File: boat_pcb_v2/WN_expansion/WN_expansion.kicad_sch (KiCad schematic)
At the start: 3 parts, among them J16 TSW-108-07-F-D, J17 TSW-108-07-F-D, J18 TSW-108-07-F-D

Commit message: cleaned up expansion board
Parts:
- added C20, C26: 1µ, 100V, WaterNet Footprints:CAPC2012X145N, symbol Device:C
- added C27, C28: 1µ, 25V, WaterNet26 Footprints:CAPC2012X145N, symbol Device:C
- added D4: USBLC6-2SC6, Package_TO_SOT_SMD:SOT-23-6, symbol Power_Protection:USBLC6-2SC6
- added J1, J2: Conn_02x10_Odd_Even, symbol Connector_Generic:Conn_02x10_Odd_Even
- added J19: TSW-108-07-F-D, WaterNet26 Library:SAMTEC_TSW-108-07-F-D, symbol WaterNet26 Library:TSW-108-07-F-D
- added J20: USB4120-03-C_REVA6, WaterNet26 Footprints:GCT_USB4120-03-C_REVA6, symbol WaterNet26 Library:USB4120-03-C_REVA6
- added JP2, JP3: B04B-PASK-1, WaterNet Footprints:B04B-PASK-1, symbol WaterNet Library:B04B-PASK-1_1
- added L6: 3.3µ, WaterNet26 Footprints:INDC1608X95N, symbol Device:L
- added R25, R26: 5.1K, WaterNet26 Footprints:RESC1508X55N, symbol WaterNet26 Library:RMCF0603FT5K10
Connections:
- net +3.3V: now also J18.02, J18.06, J18.10, J18.14
- net GND: now also J18.01, J18.05, J18.09, J18.13, C20.2, C26.2, C27.2, C28.2, D4.2 (GND), J20.A1 (GND_A), J20.A12 (GND_A), J20.B1 (GND_B), J20.B12 (GND_B), J20.S1 (SHIELD), J20.S2 (SHIELD), J20.S3 (SHIELD), J20.S4 (SHIELD), JP2.1, JP3.1, R25.1, R26.1
- net SDA: now reaches J18.03
- net SDA: now also J18.07, J18.11, J18.15
- net SCL: now reaches J18.04
- net SCL: now also J18.08, J18.12, J18.16
- new net: D4.1 (I/O1), J20.A7 (D1-), J20.B7 (D2-)
- new net: D4.3 (I/O2), J20.A6 (D1+), J20.B6 (D2+)
- new net: J20.A5 (CC1), R25.2
- new net: J20.B5 (CC2), R26.2
- new net +12ACC: J19.01, J19.02, J19.03, J19.04, J19.05, J19.06, J19.07, J19.08, J19.09, J19.10, J19.11, J19.12, J19.13, J19.14, J19.15, J19.16
- new net +3V3: C20.1, C26.1, JP2.2, JP3.2
- new net +VBUSF_1: C28.1, L6.2
- new net I2C1_SCL: JP2.4, JP3.4
- new net I2C1_SDA: JP2.3, JP3.3
- new net USB_D+: D4.4 (I/O2)
- new net USB_D-: D4.6 (I/O1)
- new net VBUS_A: C27.1, J20.A4 (VBUS_A), J20.A9 (VBUS_A), J20.B4 (VBUS_B), J20.B9 (VBUS_B), L6.1
- no-connect marks 0 -> 2
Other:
- note added: "Expansion Headers"
- note added: "I2C Header"
- note added: "I2C QWIIC CONN"
- note added: "Power Headers"
- note added: "USB-C Connector"
- moved on the sheet: J16, J17, J18

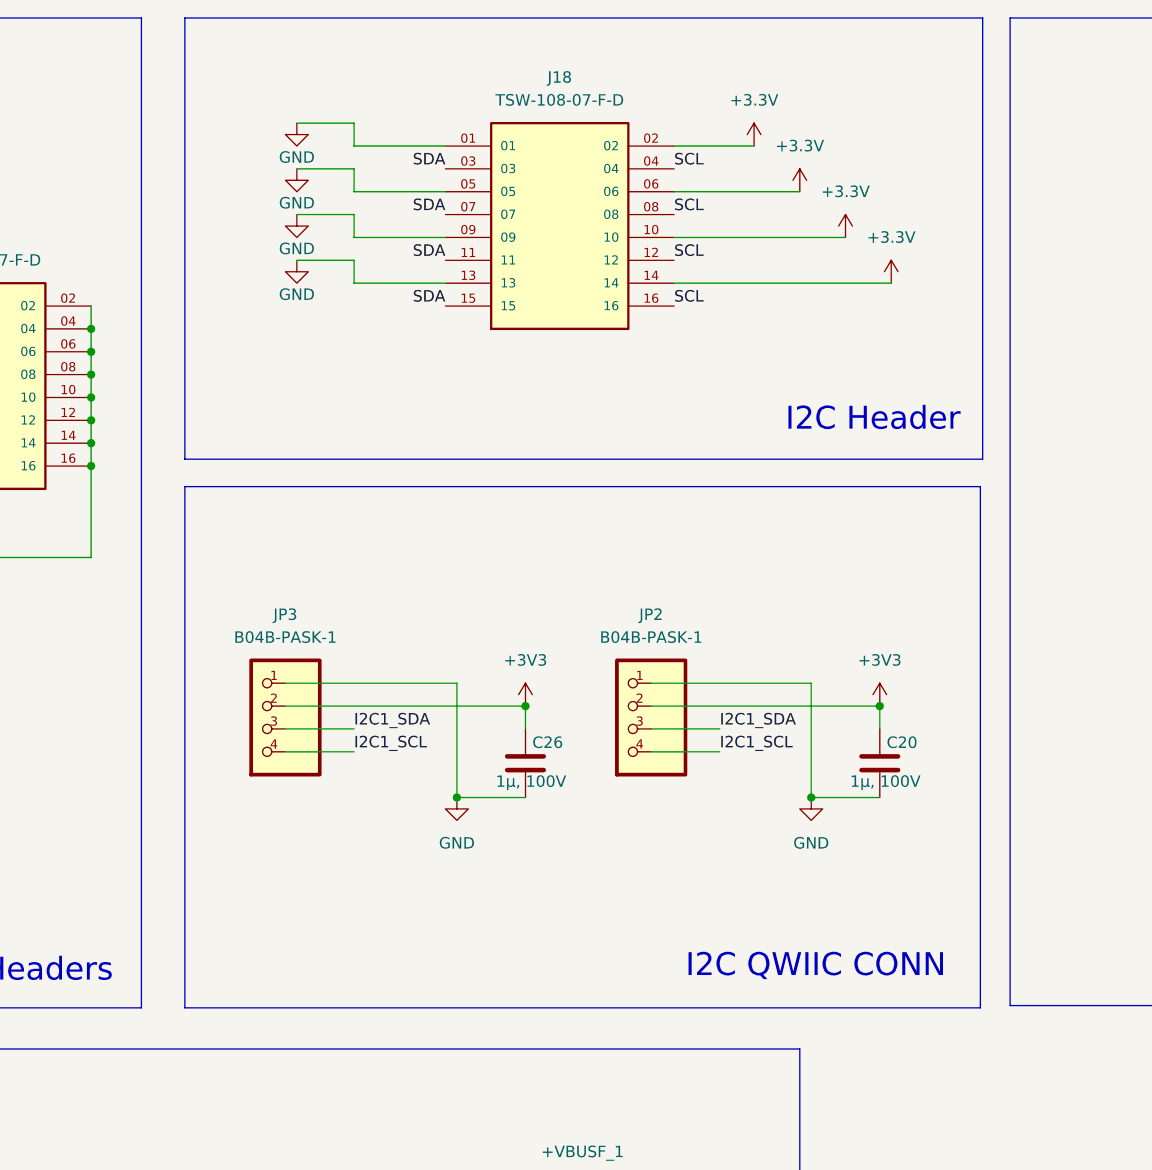
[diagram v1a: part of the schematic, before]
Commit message: minor updates related to board layout
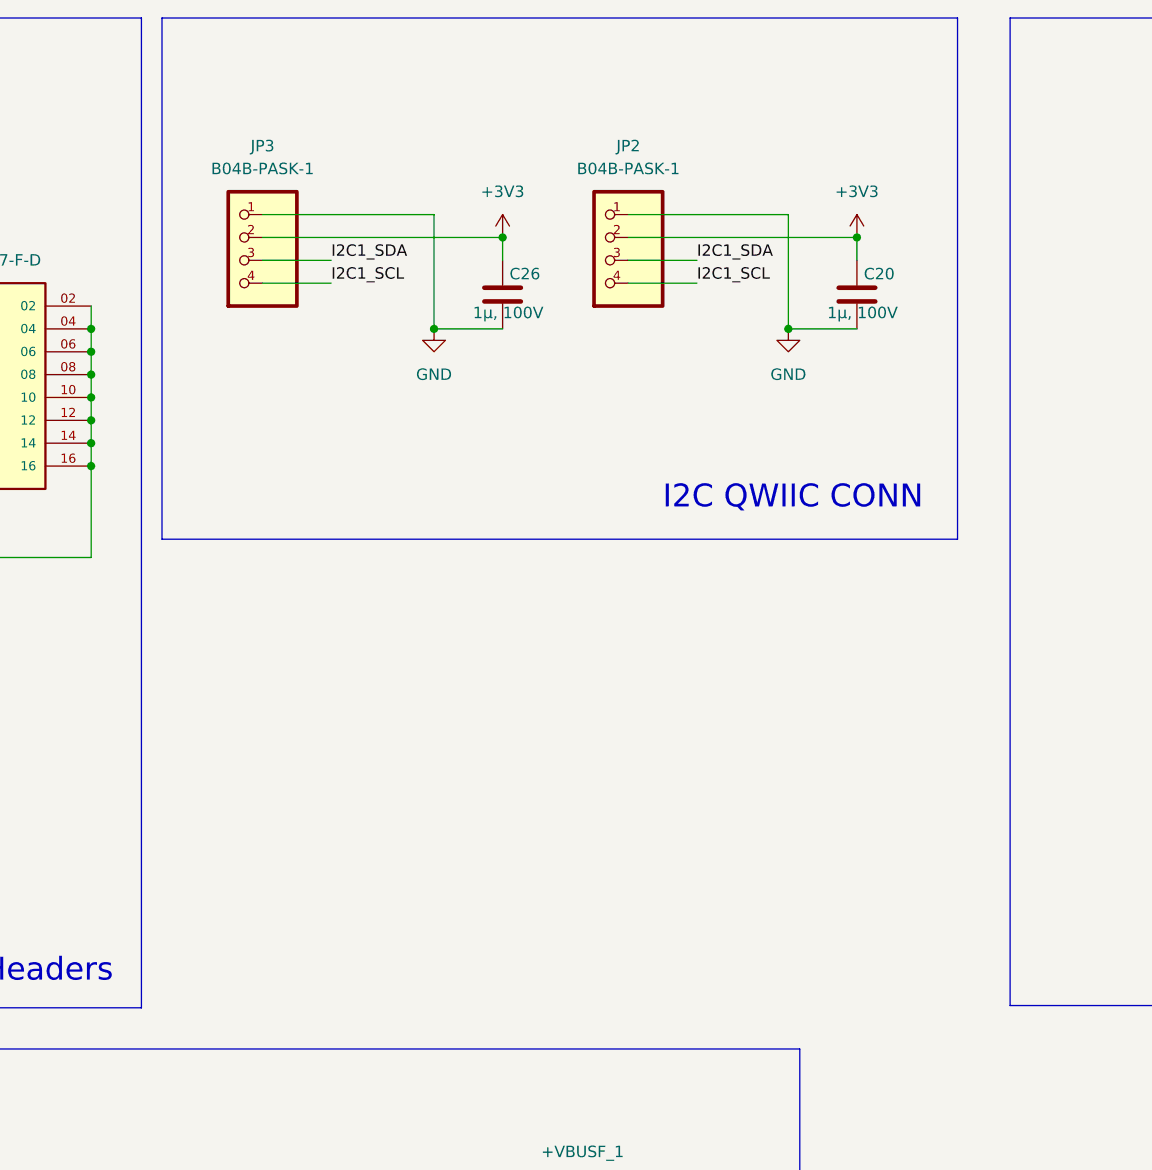
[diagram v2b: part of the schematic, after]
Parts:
- removed J18: TSW-108-07-F-D, WaterNet26 Library:SAMTEC_TSW-108-07-F-D, symbol WaterNet26 Library:TSW-108-07-F-D
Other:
- note removed: "I2C Header"
- moved on the sheet: C20, C26, JP2, JP3
